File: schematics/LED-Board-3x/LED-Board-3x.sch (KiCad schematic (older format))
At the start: 4 parts, among them P1 CONN_02X04

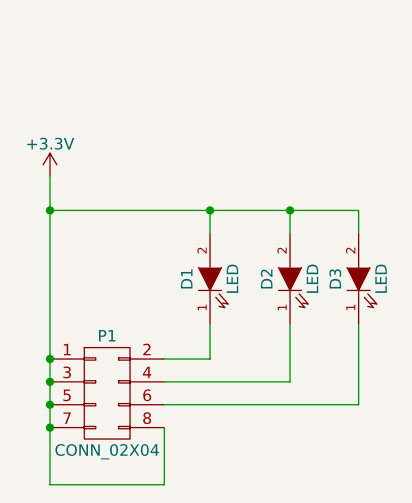
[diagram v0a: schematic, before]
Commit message: schematics: update LED connections, use 4x resistor arrays
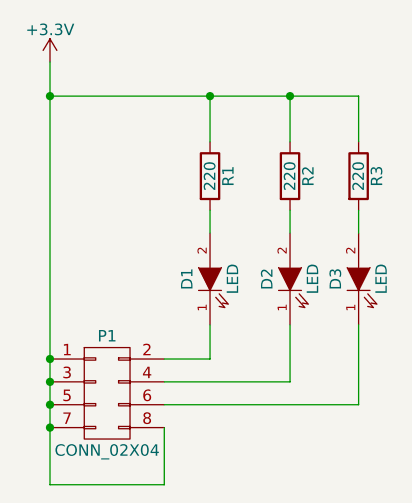
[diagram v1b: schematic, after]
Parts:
- added R1, R2, R3: 220, symbol R
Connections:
- net +3V3: now also R1.1, R2.1, R3.1; no longer D1.2 (A), D2.2 (A), D3.2 (A)
- new net: D1.2 (A), R1.2
- new net: D2.2 (A), R2.2
- new net: D3.2 (A), R3.2
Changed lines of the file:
@@
 $EndComp
 Wire Wire Line
-	3500 2050 3500 3400
+	3500 1550 3500 1700
+Wire Wire Line
+	3500 1700 3500 2850
+Wire Wire Line
+	3500 2850 3500 2950
+Wire Wire Line
+	3500 2950 3500 3050
+Wire Wire Line
+	3500 3050 3500 3150
+Wire Wire Line
+	3500 3150 3500 3400
 Connection ~ 3500 2950
 Connection ~ 3500 3050
@@
 Connection ~ 3500 3150
 $Comp
-L +3.3V #PWR01
+L +3.3V #PWR1
 U 1 1 55C870D4
-P 3500 2050
-F 0 "#PWR01" H 3500 1900 50  0001 C CNN
-F 1 "+3.3V" H 3500 2190 50  0000 C CNN
-F 2 "" H 3500 2050 60  0000 C CNN
-F 3 "" H 3500 2050 60  0000 C CNN
-	1    3500 2050
+P 3500 1550
+F 0 "#PWR1" H 3500 1400 50  0001 C CNN
+F 1 "+3.3V" H 3500 1690 50  0000 C CNN
+F 2 "" H 3500 1550 60  0000 C CNN
+F 3 "" H 3500 1550 60  0000 C CNN
+	1    3500 1550
 	1    0    0    -1
 $EndComp
@@
 	4850 2200 4850 2300
 Wire Wire Line
-	3500 2200 4850 2200
-Connection ~ 3500 2200
+	4550 2200 4550 2300
 Wire Wire Line
-	4550 2300 4550 2200
-Connection ~ 4550 2200
+	4200 2200 4200 2300
+$Comp
+L R R1
+U 1 1 55D5073B
+P 4200 2050
+F 0 "R1" V 4280 2050 50  0000 C CNN
+F 1 "220" V 4200 2050 50  0000 C CNN
+F 2 "" V 4130 2050 30  0000 C CNN
+F 3 "" H 4200 2050 30  0000 C CNN
+	1    4200 2050
+	1    0    0    -1
+$EndComp
+$Comp
+L R R2
+U 1 1 55D50785
+P 4550 2050
+F 0 "R2" V 4630 2050 50  0000 C CNN
+F 1 "220" V 4550 2050 50  0000 C CNN
+F 2 "" V 4480 2050 30  0000 C CNN
+F 3 "" H 4550 2050 30  0000 C CNN
+	1    4550 2050
+	1    0    0    -1
+$EndComp
+$Comp
+L R R3
+U 1 1 55D507BB
+P 4850 2050
+F 0 "R3" V 4930 2050 50  0000 C CNN
+F 1 "220" V 4850 2050 50  0000 C CNN
+F 2 "" V 4780 2050 30  0000 C CNN
+F 3 "" H 4850 2050 30  0000 C CNN
+	1    4850 2050
+	1    0    0    -1
+$EndComp
 Wire Wire Line
-	4200 2300 4200 2200
-Connection ~ 4200 2200
+	3500 1700 4200 1700
+Wire Wire Line
+	4200 1700 4550 1700
+Wire Wire Line
+	4550 1700 4850 1700
+Wire Wire Line
+	4850 1700 4850 1900
+Connection ~ 3500 1700
+Wire Wire Line
+	4550 1900 4550 1700
+Connection ~ 4550 1700
+Wire Wire Line
+	4200 1900 4200 1700
+Connection ~ 4200 1700
 $EndSCHEMATC

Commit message: Schematics update
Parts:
- D1: value LED -> LED1
- D2: value LED -> LED2
- D3: value LED -> LED3
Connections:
- net +3V3: no longer P1.3 (P3), P1.5 (P5), P1.7 (P7), P1.8 (P8)
- no-connect marks 0 -> 4
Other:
- moved on the sheet: D1, D2, D3, P1, R1, R2, R3
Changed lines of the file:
@@
 L CONN_02X04 P1
 U 1 1 55C867D7
-P 3750 3000
-F 0 "P1" H 3750 3250 50  0000 C CNN
-F 1 "CONN_02X04" H 3750 2750 50  0000 C CNN
-F 2 "Pin_Headers:Pin_Header_Straight_2x04_Pitch2.00mm" H 3750 1800 60  0001 C CNN
-F 3 "" H 3750 1800 60  0000 C CNN
-	1    3750 3000
+P 5250 4600
+F 0 "P1" H 5250 4850 50  0000 C CNN
+F 1 "CONN_02X04" H 5250 4350 50  0000 C CNN
+F 2 "Pin_Headers:Pin_Header_Straight_2x04_Pitch2.00mm" H 5250 3400 60  0001 C CNN
+F 3 "" H 5250 3400 60  0000 C CNN
+	1    5250 4600
 	1    0    0    -1
 $EndComp
 Wire Wire Line
-	3500 1550 3500 1700
-Wire Wire Line
-	3500 1700 3500 2850
-Wire Wire Line
-	3500 2850 3500 2950
-Wire Wire Line
-	3500 2950 3500 3050
-Wire Wire Line
-	3500 3050 3500 3150
-Wire Wire Line
-	3500 3150 3500 3400
-Connection ~ 3500 2950
-Connection ~ 3500 3050
-Wire Wire Line
-	3500 3400 4000 3400
-Wire Wire Line
-	4000 3400 4000 3150
-Connection ~ 3500 3150
+	5000 3950 5000 4450
 $Comp
 L +3.3V #PWR1
 U 1 1 55C870D4
-P 3500 1550
-F 0 "#PWR1" H 3500 1400 50  0001 C CNN
-F 1 "+3.3V" H 3500 1690 50  0000 C CNN
-F 2 "" H 3500 1550 60  0000 C CNN
-F 3 "" H 3500 1550 60  0000 C CNN
-	1    3500 1550
+P 5000 3950
+F 0 "#PWR1" H 5000 3800 50  0001 C CNN
+F 1 "+3.3V" H 5000 4090 50  0000 C CNN
+F 2 "" H 5000 3950 60  0000 C CNN
+F 3 "" H 5000 3950 60  0000 C CNN
+	1    5000 3950
 	1    0    0    -1
 $EndComp
-Connection ~ 3500 2850
 $Comp
 L LED D1
 U 1 1 55C87150
-P 4200 2500
-F 0 "D1" H 4200 2600 50  0000 C CNN
-F 1 "LED" H 4200 2400 50  0000 C CNN
-F 2 "LEDs:LED-5MM" H 4200 2500 60  0001 C CNN
-F 3 "" H 4200 2500 60  0000 C CNN
-	1    4200 2500
-	0    -1   -1   0
+P 5900 4300
+F 0 "D1" H 5800 4400 50  0000 C CNN
+F 1 "LED1" H 6000 4400 50  0000 C CNN
+F 2 "LEDs:LED-5MM" H 5900 4300 60  0001 C CNN
+F 3 "" H 5900 4300 60  0000 C CNN
+	1    5900 4300
+	1    0    0    -1
 $EndComp
 $Comp
 L LED D2
 U 1 1 55C871AB
-P 4550 2500
-F 0 "D2" H 4550 2600 50  0000 C CNN
-F 1 "LED" H 4550 2400 50  0000 C CNN
-F 2 "LEDs:LED-5MM" H 4550 2500 60  0001 C CNN
-F 3 "" H 4550 2500 60  0000 C CNN
-	1    4550 2500
-	0    -1   -1   0
+P 5900 4550
+F 0 "D2" H 5800 4650 50  0000 C CNN
+F 1 "LED2" H 6000 4650 50  0000 C CNN
+F 2 "LEDs:LED-5MM" H 5900 4550 60  0001 C CNN
+F 3 "" H 5900 4550 60  0000 C CNN
+	1    5900 4550
+	1    0    0    -1
 $EndComp
 $Comp
 L LED D3
 U 1 1 55C871CE
-P 4850 2500
-F 0 "D3" H 4850 2600 50  0000 C CNN
-F 1 "LED" H 4850 2400 50  0000 C CNN
-F 2 "LEDs:LED-5MM" H 4850 2500 60  0001 C CNN
-F 3 "" H 4850 2500 60  0000 C CNN
-	1    4850 2500
-	0    -1   -1   0
+P 5900 4800
+F 0 "D3" H 5800 4900 50  0000 C CNN
+F 1 "LED3" H 6000 4900 50  0000 C CNN
+F 2 "LEDs:LED-5MM" H 5900 4800 60  0001 C CNN
+F 3 "" H 5900 4800 60  0000 C CNN
+	1    5900 4800
+	1    0    0    -1
 $EndComp
 Wire Wire Line
-	4200 2700 4200 2850
-Wire Wire Line
-	4550 2700 4550 2950
-Wire Wire Line
-	4850 2700 4850 3050
-Wire Wire Line
-	4200 2850 4000 2850
-Wire Wire Line
-	4550 2950 4000 2950
-Wire Wire Line
-	4850 3050 4000 3050
-Wire Wire Line
-	4850 2200 4850 2300
-Wire Wire Line
-	4550 2200 4550 2300
-Wire Wire Line
-	4200 2200 4200 2300
+	5700 4550 5500 4550
 $Comp
 L R R1
 U 1 1 55D5073B
-P 4200 2050
-F 0 "R1" V 4280 2050 50  0000 C CNN
-F 1 "220" V 4200 2050 50  0000 C CNN
-F 2 "" V 4130 2050 30  0000 C CNN
-F 3 "" H 4200 2050 30  0000 C CNN
-	1    4200 2050
-	1    0    0    -1
+P 6300 4300
+F 0 "R1" V 6200 4300 50  0000 C CNN
+F 1 "220" V 6300 4300 50  0000 C CNN
+F 2 "" V 6230 4300 30  0000 C CNN
+F 3 "" H 6300 4300 30  0000 C CNN
+	1    6300 4300
+	0    1    1    0
 $EndComp
 $Comp
 L R R2
 U 1 1 55D50785
-P 4550 2050
-F 0 "R2" V 4630 2050 50  0000 C CNN
-F 1 "220" V 4550 2050 50  0000 C CNN
-F 2 "" V 4480 2050 30  0000 C CNN
-F 3 "" H 4550 2050 30  0000 C CNN
-	1    4550 2050
-	1    0    0    -1
+P 6300 4550
+F 0 "R2" V 6380 4550 50  0000 C CNN
+F 1 "220" V 6300 4550 50  0000 C CNN
+F 2 "" V 6230 4550 30  0000 C CNN
+F 3 "" H 6300 4550 30  0000 C CNN
+	1    6300 4550
+	0    1    1    0
 $EndComp
 $Comp
 L R R3
 U 1 1 55D507BB
-P 4850 2050
-F 0 "R3" V 4930 2050 50  0000 C CNN
-F 1 "220" V 4850 2050 50  0000 C CNN
-F 2 "" V 4780 2050 30  0000 C CNN
-F 3 "" H 4850 2050 30  0000 C CNN
-	1    4850 2050
-	1    0    0    -1
+P 6300 4800
+F 0 "R3" V 6380 4800 50  0000 C CNN
+F 1 "220" V 6300 4800 50  0000 C CNN
+F 2 "" V 6230 4800 30  0000 C CNN
+F 3 "" H 6300 4800 30  0000 C CNN
+	1    6300 4800
+	0    1    1    0
 $EndComp
+NoConn ~ 5000 4550
+NoConn ~ 5000 4650
+NoConn ~ 5000 4750
+NoConn ~ 5500 4750
 Wire Wire Line
-	3500 1700 4200 1700
+	6100 4800 6150 4800
 Wire Wire Line
-	4200 1700 4550 1700
+	6100 4300 6150 4300
 Wire Wire Line
-	4550 1700 4850 1700
+	5500 4450 5600 4450
 Wire Wire Line
-	4850 1700 4850 1900
-Connection ~ 3500 1700
+	5600 4450 5600 4300
 Wire Wire Line
-	4550 1900 4550 1700
-Connection ~ 4550 1700
+	5600 4300 5700 4300
 Wire Wire Line
-	4200 1900 4200 1700
-Connection ~ 4200 1700
+	5500 4650 5600 4650
+Wire Wire Line
+	5600 4650 5600 4800
+Wire Wire Line
+	5600 4800 5700 4800
+Wire Wire Line
+	6100 4550 6150 4550
+Wire Wire Line
+	6450 4800 6600 4800
+Wire Wire Line
+	6600 4800 6600 4050
+Wire Wire Line
+	6600 4050 5000 4050
+Connection ~ 5000 4050
+Wire Wire Line
+	6450 4300 6600 4300
+Connection ~ 6600 4300
+Wire Wire Line
+	6450 4550 6600 4550
+Connection ~ 6600 4550
 $EndSCHEMATC
